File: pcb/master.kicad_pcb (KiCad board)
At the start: 2 copper layers, 112.5 x 25 mm, 67 parts, among them J1 USB_C_Receptacle_USB2.0_16P, J2 Display Connector Input, J3 SSD1322 30-Pin Connector, J4 USB_C_Receptacle_USB2.0_16P, J5 Display Connector Output, J6 Micro_SD_Card, U1 ESP32-S3-WROOM-1, U2 AP2112K-3.3, U3 MT3608, U4 AP2112K-3.3, U5 ESP32-S3-WROOM-1

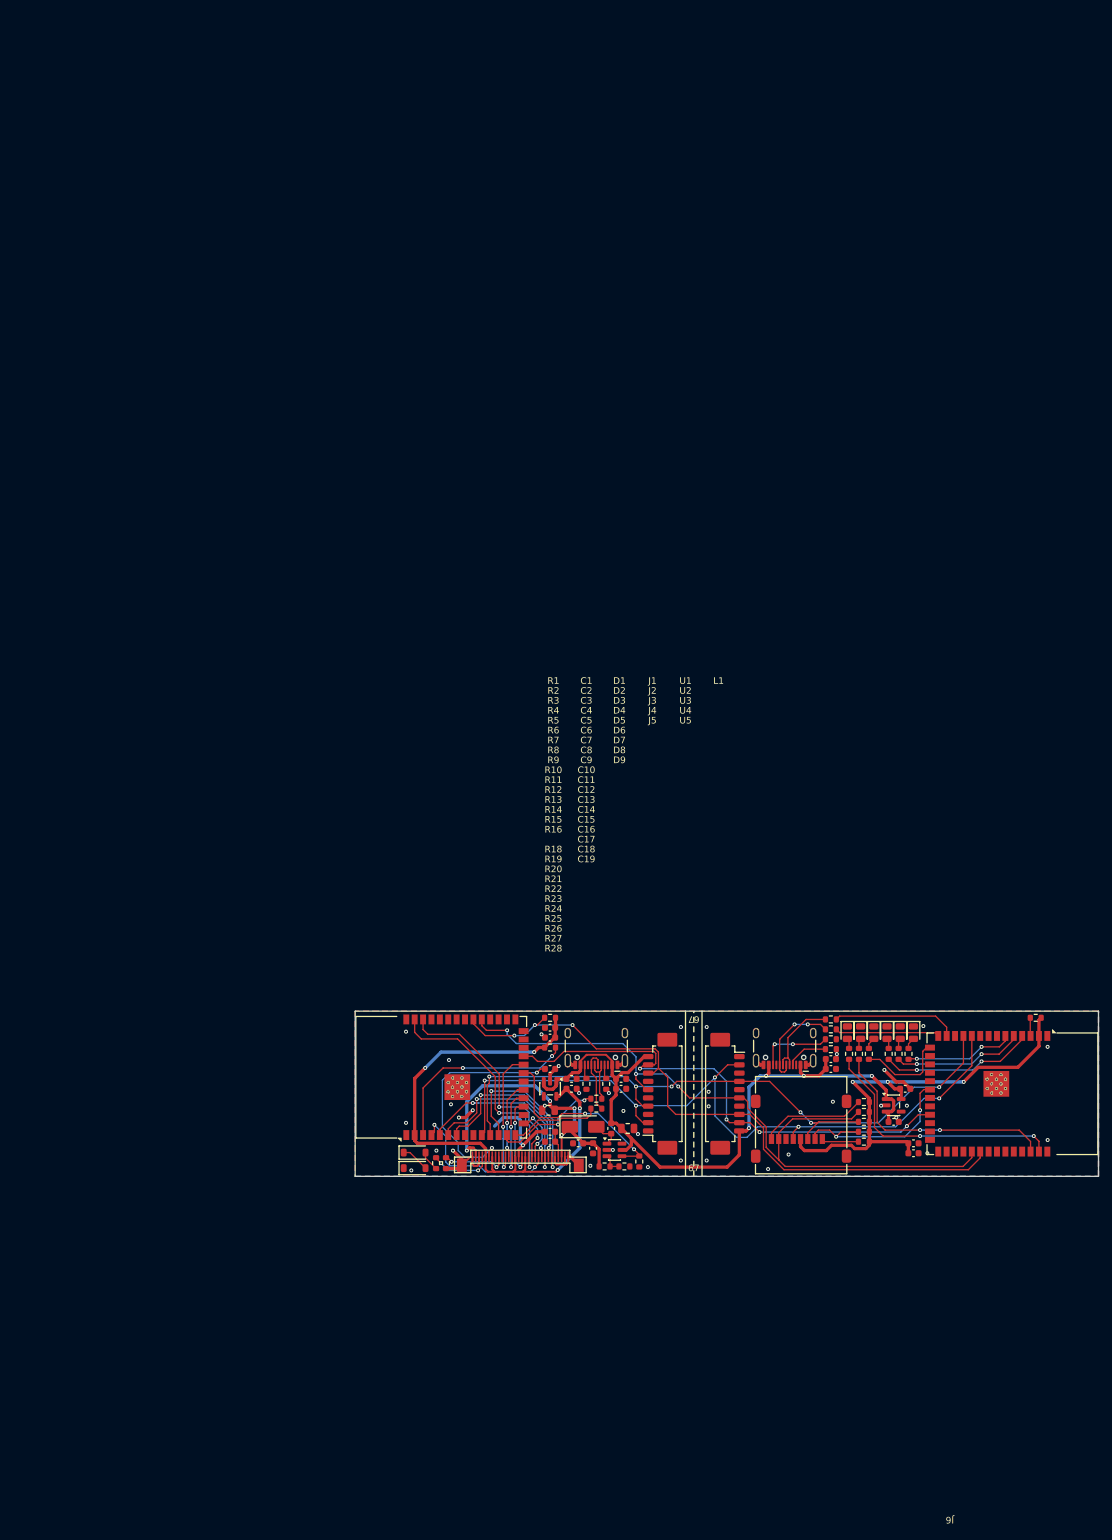
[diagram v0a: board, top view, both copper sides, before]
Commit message: Master board PCB routing
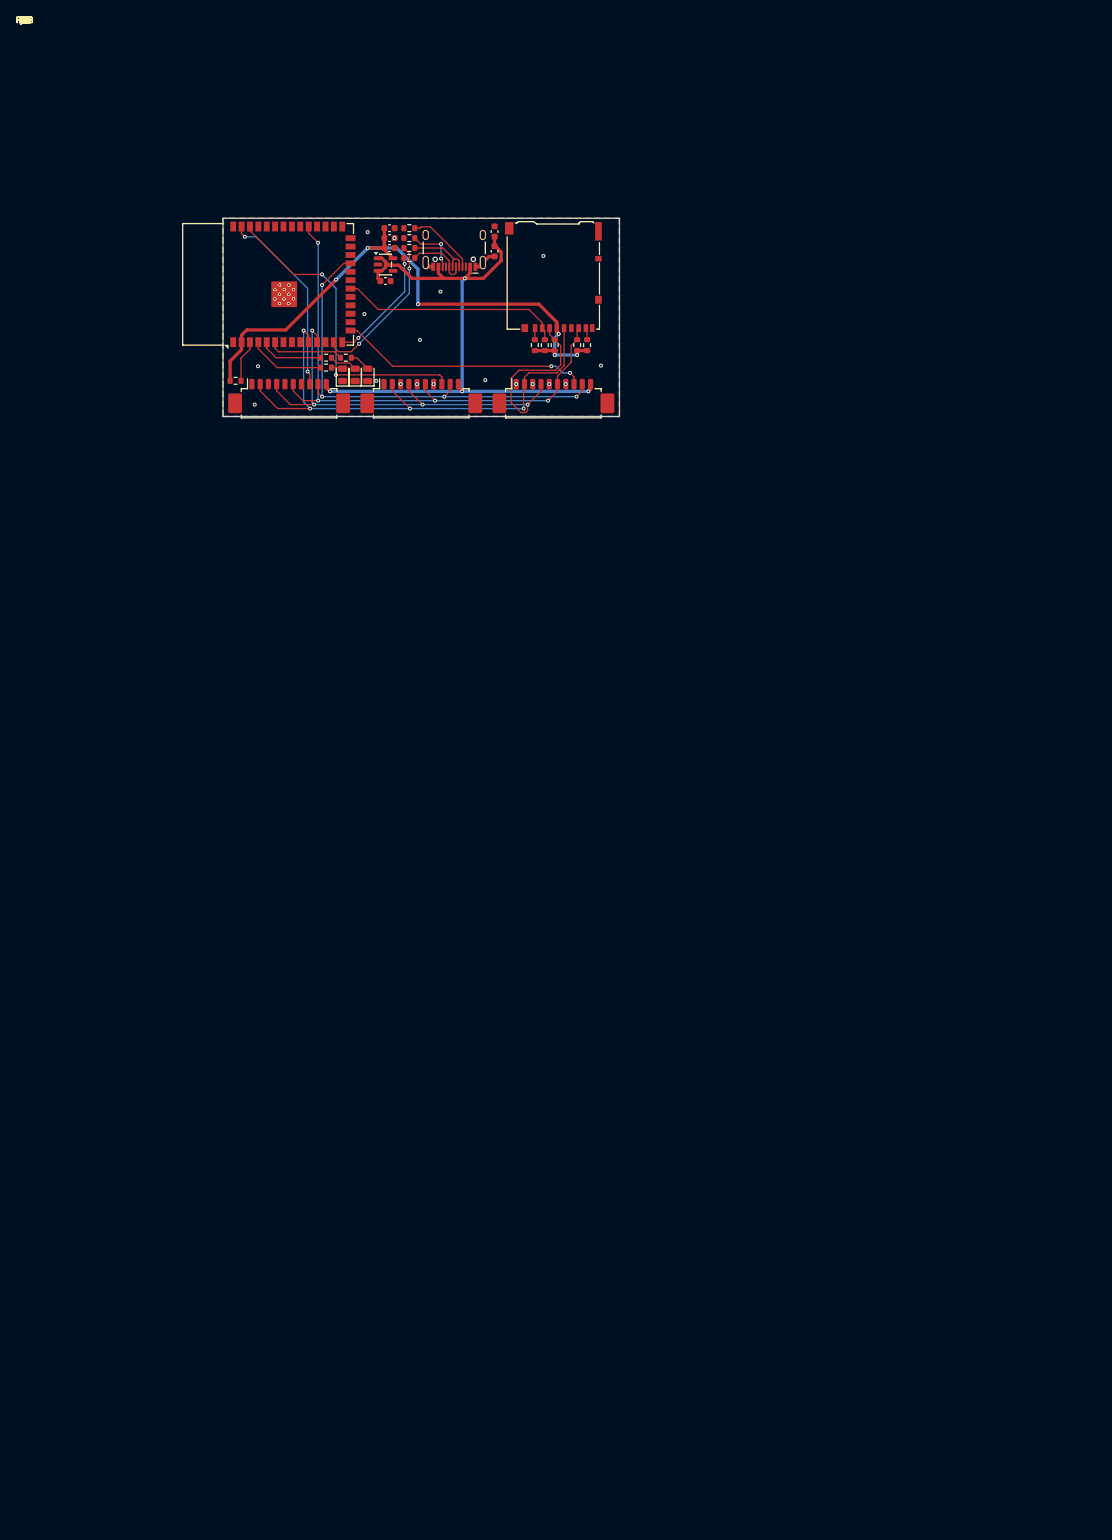
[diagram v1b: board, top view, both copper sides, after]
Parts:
- removed C14: 1uF, Capacitor_SMD:C_0603_1608Metric
- removed C15: 2.2uF, Capacitor_SMD:C_0603_1608Metric
- removed C16, C18: 10uF, Capacitor_SMD:C_0603_1608Metric
- removed C17, C19: 0.1uF, Capacitor_SMD:C_0603_1608Metric
- removed the C3 at (79.5, 158.8)
- removed the C4 at (79.5, 168.2)
- removed the C5 at (79.5, 169.8)
- removed the C6 at (83.8, 170.0)
- removed C7: 0.1uF (25V), Capacitor_SMD:C_0603_1608Metric
- removed C8: 22uF, Capacitor_SMD:C_0805_2012Metric
- removed C9: 22uF (25V), Capacitor_SMD:C_0805_2012Metric
- removed the D1 at (59.0, 171.4)
- removed the D2 at (59.0, 173.8)
- removed the D3 at (84.5, 167.5)
- removed D4: Red LED, LED_SMD:LED_0805_2012Metric
- removed D5: Yellow LED, LED_SMD:LED_0805_2012Metric
- removed D6: Green LED, LED_SMD:LED_0805_2012Metric
- removed the J2 at (96.8, 162.5)
- removed J6: Micro_SD_Card, Connector_Card:microSD_HC_Molex_47219-2001
- removed L1: 22uH (or 10uH), Inductor_SMD:L_0603_1608Metric
- removed the R1 at (63.8, 173.0)
- removed the R10 at (79.5, 151.0)
- removed the R12 at (85.0, 161.0)
- removed the R13 at (88.0, 161.0)
- removed R14, R15: 22R, Resistor_SMD:R_0603_1608Metric
- removed R16: 10k, Resistor_SMD:R_0603_1608Metric
- removed the R2 at (62.2, 173.0)
- removed R23, R24, R25: 470R, Resistor_SMD:R_0603_1608Metric
- removed the R3 at (87.8, 173.5)
- removed the R4 at (90.8, 173.5)
- removed the R9 at (93.0, 172.8)
- removed the U1 at (63.0, 160.0)
- removed the U2 at (79.5, 161.8)
- removed U3: MT3608, Package_TO_SOT_SMD:SOT-23-6
- added J4: Display Connector Output, Connector_Molex:Molex_PicoBlade_53261-1071_1x10-1MP_P1.25mm_Horizontal, F.Cu at (80.0, 57.5)
- J1: value USB_C_Receptacle_USB2.0_16P -> Micro_SD_Card_Det2; footprint Connector_USB:USB_C_Receptacle_HCTL_HC-TYPE-C-16P-01A -> Connector_Card:microSD_HC_Hirose_DM3AT-SF-PEJM5
- J3: value SSD1322 30-Pin Connector -> Display Connector Output; footprint SSD1322:ssd1322 -> Connector_Molex:Molex_PicoBlade_53261-1071_1x10-1MP_P1.25mm_Horizontal
- moved U2 166.5 mm to (36.8, 40.0), turned to 90 degrees
- moved C5 159.6 mm to (55.2, 31.5)
- moved C6 159.6 mm to (55.2, 33.0)
- moved R13 154.8 mm to (31.9, 54.6), turned to 0 degrees
- moved C4 149.3 mm to (55.2, 34.5)
- moved C3 148.7 mm to (54.6, 39.5)
- moved U1 148.7 mm to (54.6, 37.0)
- moved R10 139.7 mm to (58.2, 31.5), turned to 180 degrees
- moved R9 137.0 mm to (58.2, 33.0), turned to 180 degrees
- moved R7 136.4 mm to (45.6, 51.1), turned to 180 degrees
- moved R3 135.5 mm to (48.6, 51.1), turned to 180 degrees
- moved C1 135.2 mm to (71.1, 32.0), turned to 90 degrees
- moved R8 134.3 mm to (45.6, 52.6), turned to 180 degrees
- moved C2 133.8 mm to (71.1, 35.0), turned to -90 degrees
- moved R11 133.0 mm to (58.2, 34.5), turned to 180 degrees
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- renumbered C10 to C1, C11 to C2, C1 to C3, C2 to C4, C12 to C5, C13 to C6, D9 to D1, D8 to D2, D7 to D3, J5 to J2, J4 to J5, R21 to R1, R6 to R10, R7 to R11, R8 to R12, R11 to R13, R20 to R2, R28 to R3, R19 to R4, R22 to R5, R18 to R6, R27 to R7, R26 to R8, R5 to R9, U4 to U1, U5 to U2
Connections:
- J2 pad 8: /CS_DISPLAY -> /CS_DISPLAY_1
- J3 pad 10: /ESP32 for SSD1322/GPIO4 -> +5V
- J3 pad 2: GND -> /CLK
- J3 pad 3: +12V -> GND
- J3 pad 4: Net-(J3-VCOMH) -> /MOSI
- J3 pad 6: /ESP32 for SSD1322/GPIO8 -> /MISO
- J3 pad 7: /ESP32 for SSD1322/GPIO7 -> GND
- J3 pad 8: /ESP32 for SSD1322/GPIO6 -> /CS_DISPLAY_2
- J3 pad 9: /ESP32 for SSD1322/GPIO5 -> /WAKE
- R1 pad 2: Net-(J6-DAT1) -> Net-(J1-DAT1)
- R5 pad 2: /CS_SD -> /Master ESP32/GPIO12
- R6 pad 2: Net-(J6-DAT2) -> Net-(J1-DAT2)
- U2 pad 15: /Master ESP32/GPIO3 -> /CS_DISPLAY_3
- U2 pad 20: /CS_SD -> /Master ESP32/GPIO12
- U2 pad 32: /CS_DISPLAY -> /Master ESP32/GPIO39
- U2 pad 38: /Master ESP32/GPIO2 -> /CS_DISPLAY_2
- U2 pad 39: /Master ESP32/GPIO1 -> /CS_DISPLAY_1
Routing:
- net /CS_DISPLAY: track 99.2 -> 0.00 mm, vias 3 -> 0
- net /ESP32 for SSD1322/3V3: track 85.9 -> 0.00 mm, vias 4 -> 0
- net +12V: track 48.0 -> 0.00 mm, vias 4 -> 0
- net /CS_DISPLAY_2: track 0.00 -> 47.6 mm, vias 0 -> 2
- net GND: track 48.6 -> 4.94 mm, vias 38 -> 18
- net /Master ESP32/GPIO1: track 39.2 -> 0.00 mm, vias 2 -> 0
- net /CS_DISPLAY_3: track 0.00 -> 37.8 mm, vias 0 -> 2
- net /Master ESP32/GPIO2: track 36.6 -> 0.00 mm, vias 2 -> 0
- net /ESP32 for SSD1322/GPIO1: track 36.4 -> 0.00 mm, vias 2 -> 0
- net Net-(J3-VDD): track 35.5 -> 0.00 mm, vias 2 -> 0
- net /CLK: track 112.2 -> 78.3 mm, vias 5 -> 4
- net /Master ESP32/GPIO12: track 0.00 -> 33.9 mm
- net /ESP32 for SSD1322/GPIO2: track 33.3 -> 0.00 mm, vias 2 -> 0
- net Net-(U1-EN): track 30.2 -> 0.00 mm, vias 2 -> 0
- net /ESP32 for SSD1322/GPIO13: track 29.2 -> 0.00 mm, vias 2 -> 0
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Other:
- board size 112.5 x 25 mm -> 60 x 30 mm
- board text added: "ESP32 RC Bus Controller"
- board text added: "Jonathan Ho 2026-03-12"
- board text removed: "67"
- board text removed: "ESP32 1:13 RC Bus System"
- board text removed: "ESP32 SSD1322 Display Driver"
- board text removed: "Jonathan Ho 2026-01-28"
